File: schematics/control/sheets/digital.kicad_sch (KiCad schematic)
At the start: 17 parts, among them U1 Pico, U12 TL072, U3 MCP4822

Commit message: Updated VCA
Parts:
- added C32, C33: 100n, Shmoergh_Manual_PCB:C_Disc_D5.0mm_W2.5mm_P2.50mm, symbol Device:C
- added C34, C35, C36, C37: 100n, symbol Device:C
- added J_ADC_INPUTS1, J_BUTTON_INPUTS2: Conn_01x08_Male, Shmoergh_Manual_PCB:NSL25_01x08_Vertical, symbol Connector:Conn_01x08_Male
- added RV_ENV_GAIN1: 200k, symbol Device:R_Potentiometer_Trim
- added TP_ENV_OUT1, TP_FILT_MOD1: TestPoint, symbol Connector:TestPoint
- added U13, U14: CD4051B, Shmoergh_Manual_PCB:DIP-16_W7.62mm, symbol Analog_Switch:CD4051B
- R54: value 100k -> 22k
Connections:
- net +5V: now also C32.1, C33.1, U13.16 (VDD), U14.16 (VDD)
- net ENVELOPE: now also RV_ENV_GAIN1.1, TP_ENV_OUT1.1; no longer R54.2
- net FILTER_MOD: now also TP_FILT_MOD1.1
- net GND: now also C32.2, C33.2, C34.2, C35.2, C36.2, C37.2, U13.6 (INH), U13.7 (VEE), U13.8 (VSS), U14.6 (INH), U14.7 (VEE), U14.8 (VSS)
- net MUX_BTN: now reaches U1.11 (GPIO8)
- net MUX_BTN: now also U14.3 (X)
- net MUX_ADC: now reaches U1.31 (GPIO26_ADC0)
- net MUX_ADC: now also U13.3 (X)
- net MUX_A: now reaches U1.4 (GPIO2)
- net MUX_A: now also U13.11 (A), U14.11 (A)
- net MUX_B: now reaches U1.5 (GPIO3)
- net MUX_B: now also U13.10 (B), U14.10 (B)
- net MUX_C: now reaches U1.6 (GPIO4)
- net MUX_C: now also U13.9 (C), U14.9 (C)
- new net: R54.2, RV_ENV_GAIN1.2, RV_ENV_GAIN1.3
- new net: J_ADC_INPUTS1.8 (Pin_8), U13.4 (X7)
- new net: J_BUTTON_INPUTS2.8 (Pin_8), U14.4 (X7)
- new net DETUNE: J_BUTTON_INPUTS2.5 (Pin_5), U14.1 (X4)
- new net GLIDE: J_BUTTON_INPUTS2.4 (Pin_4), U14.12 (X3)
- new net HOLD: J_BUTTON_INPUTS2.2 (Pin_2), U14.14 (X1)
- new net KB_TRACKING: J_BUTTON_INPUTS2.6 (Pin_6), U14.5 (X5)
- new net MODE: C35.1, J_ADC_INPUTS1.2 (Pin_2), U13.14 (X1)
- new net MODWHEEL: J_ADC_INPUTS1.7 (Pin_7), U13.2 (X6)
- new net PITCH: J_ADC_INPUTS1.6 (Pin_6), U13.5 (X5)
- new net RING: J_BUTTON_INPUTS2.3 (Pin_3), U14.15 (X2)
- new net RING_AMNT: C36.1, J_ADC_INPUTS1.3 (Pin_3), U13.15 (X2)
- new net SOFT: J_BUTTON_INPUTS2.1 (Pin_1), U14.13 (X0)
- new net SOLO_CHORD: J_BUTTON_INPUTS2.7 (Pin_7), U14.2 (X6)
- new net TUNER: J_ADC_INPUTS1.5 (Pin_5), U13.1 (X4)
- new net WAH_SRC: C37.1, J_ADC_INPUTS1.4 (Pin_4), U13.12 (X3)
- new net WAVESHAPE: C34.1, J_ADC_INPUTS1.1 (Pin_1), U13.13 (X0)
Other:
- note added: "ADC inputs ------- Waveshape (saw/sqr/mixed) Mode (mono, 3/6 para) Ring amount Wah source Global tuner Pitch Modwheel * note: square pulse width is completely analog and set externally on the UI"
- note added: "Binary inputs (on/off) ------------- Soft Hold Ring Glide Detune Keyboard tracking Solo/chord"
- note added: "Envelope maximum: about 5-12V"
- note removed: "Envelope varies between 0-8V"
- moved on the sheet: C30, C31, J_SWD_IO?, R53, R54, R55, R56, U1, U12A, U12B, U12C, U3

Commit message: Coded portamento (untested)
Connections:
- net MUX_BTN renamed MUX_BINARY
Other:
- note added: "ADC inputs ------- Waveshape (saw/sqr/mixed) Mode (mono, 3/6 para) Ring amount Wah source Global tuner Pitch (Modwheel? — This can be pure analog) * note: square pulse width is completely analog and set externally on the UI"
- note added: "ATM it's only keyboard tracking"
- note removed: "ADC inputs ------- Waveshape (saw/sqr/mixed) Mode (mono, 3/6 para) Ring amount Wah source Global tuner Pitch Modwheel * note: square pulse width is completely analog and set externally on the UI"
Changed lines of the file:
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@@
     (stroke (width 0) (type default))
   )
+  (text "ATM it's only keyboard \ntracking" (at 177.8 121.92 0)
+    (effects (font (size 1.27 1.27)) (justify left bottom))
+  )
   (text "In Purple Thunder MIDI IN is connected to GPIO9" (at 109.22 176.53 0)
     (effects (font (size 1.27 1.27)) (justify left bottom))
@@
     (effects (font (size 1.27 1.27)) (justify left bottom))
   )
-  (text "ADC inputs\n-------\nWaveshape (saw/sqr/mixed)\nMode (mono, 3/6 para)\nRing amount\nWah source\nGlobal tuner\nPitch\nModwheel\n\n* note: square pulse width \nis completely analog and\nset externally on the UI"
-    (at 181.61 43.18 0)
+  (text "ADC inputs\n-------\nWaveshape (saw/sqr/mixed)\nMode (mono, 3/6 para)\nRing amount\nWah source\nGlobal tuner\nPitch\n(Modwheel? — This can be \npure analog)\n\n* note: square pulse width \nis completely analog and\nset externally on the UI"
+    (at 180.34 52.07 0)
     (effects (font (size 1.27 1.27)) (justify left bottom))
   )
@@
     )
   )
-  (global_label "MUX_BTN" (shape input) (at 224.79 111.76 180) (fields_autoplaced)
-    (effects (font (size 1.27 1.27)) (justify right))
-    (property "Intersheetrefs" "${INTERSHEET_REFS}" (at 213.3571 111.76 0)
+  (global_label "MUX_BINARY" (shape input) (at 224.79 111.76 180) (fields_autoplaced)
+    (effects (font (size 1.27 1.27)) (justify right))
+    (property "Intersheetrefs" "${INTERSHEET_REFS}" (at 210.2727 111.76 0)
       (effects (font (size 1.27 1.27)) (justify right) hide)
     )
@@
     )
   )
-  (global_label "MUX_BTN" (shape input) (at 31.75 57.15 180) (fields_autoplaced)
-    (effects (font (size 1.27 1.27)) (justify right))
-    (property "Intersheetrefs" "${INTERSHEET_REFS}" (at 20.3171 57.15 0)
-      (effects (font (size 1.27 1.27)) (justify right) hide)
-    )
+  (global_label "MUX_BINARY" (shape input) (at 31.75 57.15 180) (fields_autoplaced)
+    (effects (font (size 1.27 1.27)) (justify right))
+    (property "Intersheetrefs" "${INTERSHEET_REFS}" (at 17.2327 57.15 0)
+      (effects (font (size 1.27 1.27)) (justify right) hide)
+    )

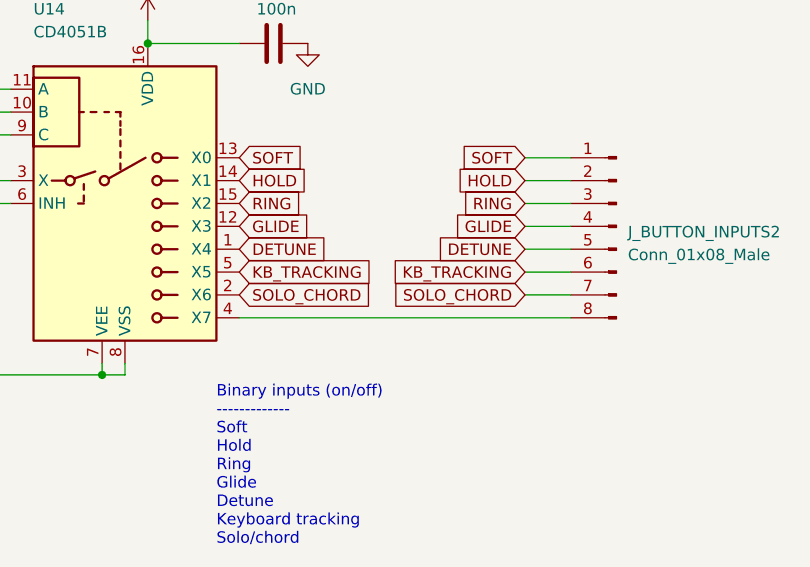
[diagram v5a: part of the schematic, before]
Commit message: Updated kb tracking for analog switch
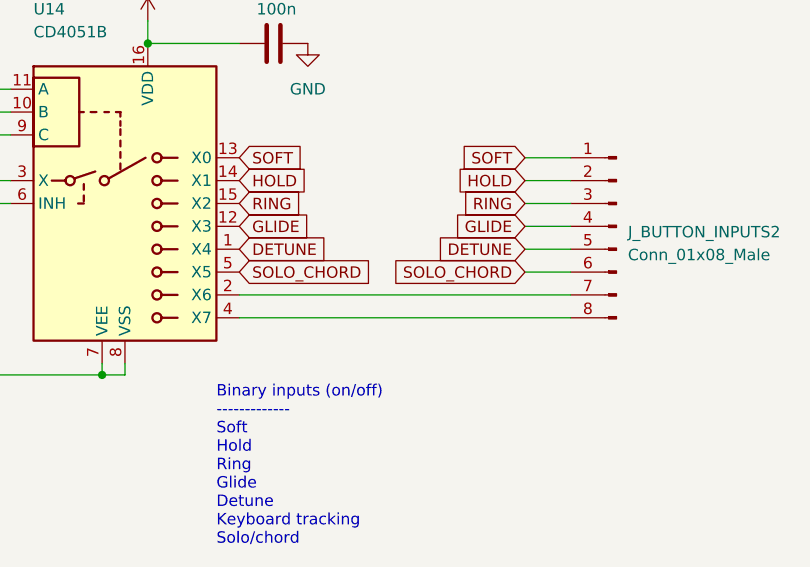
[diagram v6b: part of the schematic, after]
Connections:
- net KB_TRACKING is gone; now on net SOLO_CHORD: J_BUTTON_INPUTS2.6 (Pin_6), U14.5 (X5)
- net SOLO_CHORD: no longer J_BUTTON_INPUTS2.7 (Pin_7), U14.2 (X6)
- new net: J_BUTTON_INPUTS2.7 (Pin_7), U14.2 (X6)
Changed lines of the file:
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@@
     (stroke (width 0) (type default))
   )
-  (wire (pts (xy 283.21 124.46) (xy 288.29 124.46))
+  (wire (pts (xy 251.46 124.46) (xy 288.29 124.46))
     (stroke (width 0) (type default))
   )
@@
     )
   )
-  (global_label "SOLO_CHORD" (shape input) (at 283.21 124.46 180) (fields_autoplaced)
-    (effects (font (size 1.27 1.27)) (justify right))
-    (property "Intersheetrefs" "${INTERSHEET_REFS}" (at 267.967 124.46 0)
+  (global_label "SOLO_CHORD" (shape input) (at 283.21 121.92 180) (fields_autoplaced)
+    (effects (font (size 1.27 1.27)) (justify right))
+    (property "Intersheetrefs" "${INTERSHEET_REFS}" (at 267.967 121.92 0)
       (effects (font (size 1.27 1.27)) (justify right) hide)
     )
@@
     )
   )
-  (global_label "SOLO_CHORD" (shape input) (at 251.46 124.46 0) (fields_autoplaced)
-    (effects (font (size 1.27 1.27)) (justify left))
-    (property "Intersheetrefs" "${INTERSHEET_REFS}" (at 266.703 124.46 0)
+  (global_label "SOLO_CHORD" (shape input) (at 251.46 121.92 0) (fields_autoplaced)
+    (effects (font (size 1.27 1.27)) (justify left))
+    (property "Intersheetrefs" "${INTERSHEET_REFS}" (at 266.703 121.92 0)
       (effects (font (size 1.27 1.27)) (justify left) hide)
     )
@@
     )
   )
-  (global_label "KB_TRACKING" (shape input) (at 251.46 121.92 0) (fields_autoplaced)
-    (effects (font (size 1.27 1.27)) (justify left))
-    (property "Intersheetrefs" "${INTERSHEET_REFS}" (at 266.9449 121.92 0)
-      (effects (font (size 1.27 1.27)) (justify left) hide)
-    )
-  )
   (global_label "DAC_CS" (shape input) (at 99.06 113.03 180) (fields_autoplaced)
     (effects (font (size 1.27 1.27)) (justify right))
@@
       (effects (font (size 1.27 1.27)) (justify right) hide)
     )
-  )
-  (global_label "KB_TRACKING" (shape input) (at 283.21 121.92 180) (fields_autoplaced)
-    (effects (font (size 1.27 1.27)) (justify right))
-    (property "Intersheetrefs" "${INTERSHEET_REFS}" (at 267.7251 121.92 0)
-      (effects (font (size 1.27 1.27)) (justify right) hide)
-    )

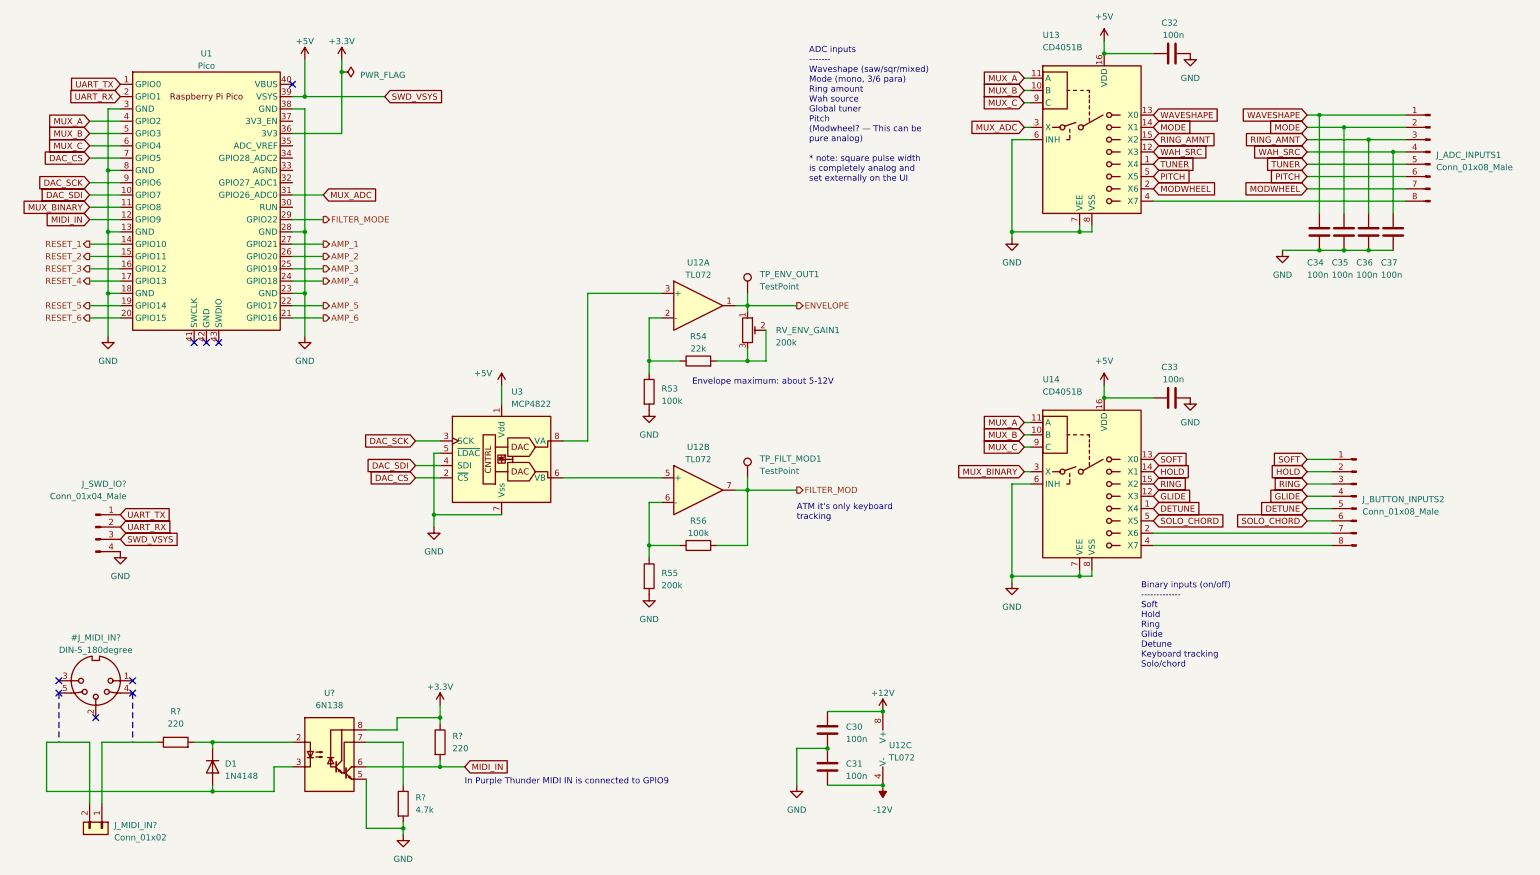
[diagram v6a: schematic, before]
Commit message: Added all UI components to schematics
- digital UI
- filter UI
- updated voice interface connection
- simplified schematics a lot
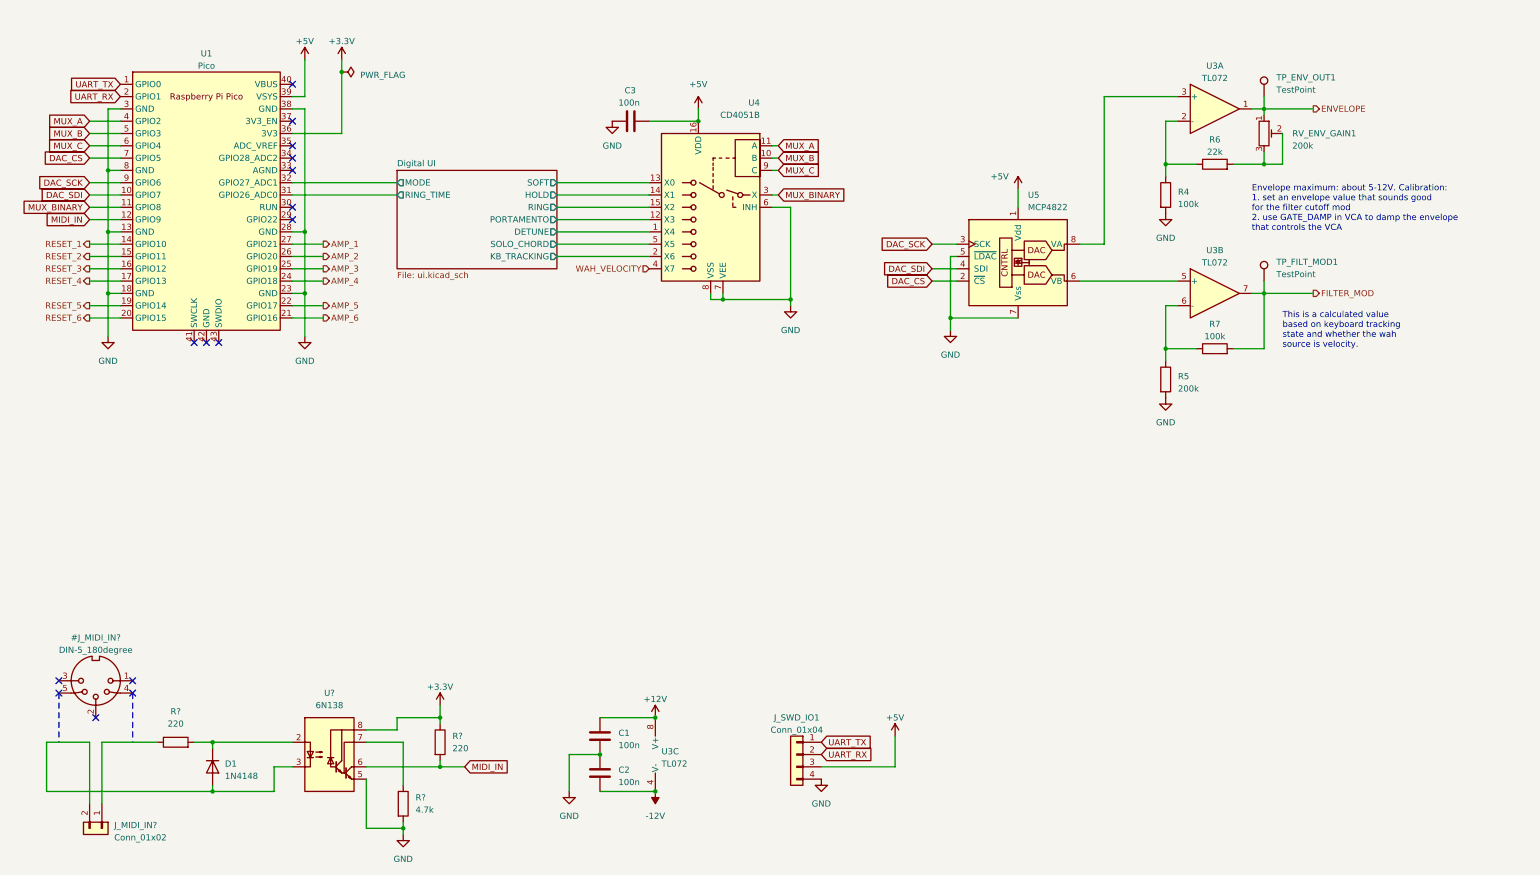
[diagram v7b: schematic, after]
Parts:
- removed C32: 100n, Shmoergh_Manual_PCB:C_Disc_D5.0mm_W2.5mm_P2.50mm, symbol Device:C
- removed C34, C35, C36, C37: 100n, symbol Device:C
- removed J_ADC_INPUTS1, J_BUTTON_INPUTS2: Conn_01x08_Male, Shmoergh_Manual_PCB:NSL25_01x08_Vertical, symbol Connector:Conn_01x08_Male
- removed J_SWD_IO?: Conn_01x04_Male, Connector_PinHeader_2.54mm:PinHeader_1x04_P2.54mm_Vertical, symbol Connector:Conn_01x04_Male
- removed U13: CD4051B, Shmoergh_Manual_PCB:DIP-16_W7.62mm, symbol Analog_Switch:CD4051B
- added J_SWD_IO1: Conn_01x04, symbol Connector_Generic:Conn_01x04
- C3: renamed from C33; footprint Shmoergh_Manual_PCB:C_Disc_D5.0mm_W2.5mm_P2.50mm -> (none)
- D1: footprint Diode_THT:D_DO-35_SOD27_P7.62mm_Horizontal -> (none)
- J_MIDI_IN?: footprint Shmoergh_Custom_Footprints:NSL25_01x02_Vertical -> (none)
- R? (x3): footprint Shmoergh_Custom_Footprints:R_Axial_DIN0207_L6.3mm_D2.5mm_P7.62mm_Horizontal -> (none)
- U1: footprint MCU_RaspberryPi_and_Boards:RPi_Pico_SMD_TH -> (none)
- U4: renamed from U14; footprint Shmoergh_Manual_PCB:DIP-16_W7.62mm -> (none)
- U5: renamed from U3; footprint Package_DIP:DIP-8_W7.62mm -> (none)
- U?: footprint Package_DIP:DIP-8_W7.62mm -> (none)
- renumbered C30 to C1, C31 to C2, R53 to R4, R55 to R5, R54 to R6, R56 to R7, U12 to U3
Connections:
- net +5V: now also J_SWD_IO1.3 (Pin_3)
- net GND: now also J_SWD_IO1.4 (Pin_4)
- net UART_RX: now also J_SWD_IO1.2 (Pin_2)
- net UART_TX: now also J_SWD_IO1.1 (Pin_1)
- net Digital UI/MODE: now reaches U1.32 (GPIO27_ADC1)
- net Digital UI/KB_TRACKING: now reaches U4.2 (X6)
- net WAH_VELOCITY: now reaches U4.4 (X7)
- net DETUNE renamed Digital UI/DETUNE
- net FILTER_MODE: no longer names the net of U1.29 (GPIO22)
- net GLIDE renamed Digital UI/PORTAMENTO
- net HOLD renamed Digital UI/HOLD
- net MUX_ADC renamed Digital UI/RING_TIME
- net RING renamed Digital UI/RING
- net SOFT renamed Digital UI/SOFT
- net SOLO_CHORD renamed Digital UI/SOLO_CHORD
- no-connect marks 9 -> 15
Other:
- added sheet Digital UI (ui.kicad_sch)
- note added: "Envelope maximum: about 5-12V. Calibration: 1. set an envelope value that sounds good for the filter cutoff mod 2. use GATE_DAMP in VCA to damp the envelope that controls the VCA"
- note added: "This is a calculated value based on keyboard tracking state and whether the wah source is velocity."
- note removed: "ADC inputs ------- Waveshape (saw/sqr/mixed) Mode (mono, 3/6 para) Ring amount Wah source Global tuner Pitch (Modwheel? — This can be pure analog) * note: square pulse width is completely analog and set externally on the UI"
- note removed: "ATM it's only keyboard tracking"
- note removed: "Binary inputs (on/off) ------------- Soft Hold Ring Glide Detune Keyboard tracking Solo/chord"
- note removed: "Envelope maximum: about 5-12V"
- note removed: "In Purple Thunder MIDI IN is connected to GPIO9"
- moved on the sheet: C1, C2, C3, R4, R5, R6, R7, RV_ENV_GAIN1, TP_ENV_OUT1, TP_FILT_MOD1, U3A, U3B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

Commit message: Refined voice values
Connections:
- net AMP_1: now also U1.21 (GPIO16); no longer U1.27 (GPIO21)
- net AMP_2: now also U1.22 (GPIO17); no longer U1.26 (GPIO20)
- net AMP_3: now also U1.24 (GPIO18); no longer U1.25 (GPIO19)
- net AMP_4: now also U1.25 (GPIO19); no longer U1.24 (GPIO18)
- net AMP_5: now also U1.26 (GPIO20); no longer U1.22 (GPIO17)
- net AMP_6: now also U1.27 (GPIO21); no longer U1.21 (GPIO16)
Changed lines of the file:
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@@
     (effects (font (size 1.27 1.27)) (justify left))
   )
-  (hierarchical_label "AMP_2" (shape output) (at 80.01 67.31 0) (fields_autoplaced)
+  (hierarchical_label "AMP_2" (shape output) (at 80.01 77.47 0) (fields_autoplaced)
     (effects (font (size 1.27 1.27)) (justify left))
   )
@@
     (effects (font (size 1.27 1.27)) (justify right))
   )
-  (hierarchical_label "AMP_3" (shape output) (at 80.01 69.85 0) (fields_autoplaced)
+  (hierarchical_label "AMP_3" (shape output) (at 80.01 72.39 0) (fields_autoplaced)
     (effects (font (size 1.27 1.27)) (justify left))
   )
@@
     (effects (font (size 1.27 1.27)) (justify left))
   )
-  (hierarchical_label "AMP_1" (shape output) (at 80.01 64.77 0) (fields_autoplaced)
+  (hierarchical_label "AMP_1" (shape output) (at 80.01 80.01 0) (fields_autoplaced)
     (effects (font (size 1.27 1.27)) (justify left))
   )
@@
     (effects (font (size 1.27 1.27)) (justify right))
   )
-  (hierarchical_label "AMP_6" (shape output) (at 80.01 80.01 0) (fields_autoplaced)
+  (hierarchical_label "AMP_6" (shape output) (at 80.01 64.77 0) (fields_autoplaced)
     (effects (font (size 1.27 1.27)) (justify left))
   )
-  (hierarchical_label "AMP_4" (shape output) (at 80.01 72.39 0) (fields_autoplaced)
+  (hierarchical_label "AMP_4" (shape output) (at 80.01 69.85 0) (fields_autoplaced)
     (effects (font (size 1.27 1.27)) (justify left))
   )
@@
     (effects (font (size 1.27 1.27)) (justify right))
   )
-  (hierarchical_label "AMP_5" (shape output) (at 80.01 77.47 0) (fields_autoplaced)
+  (hierarchical_label "AMP_5" (shape output) (at 80.01 67.31 0) (fields_autoplaced)
     (effects (font (size 1.27 1.27)) (justify left))
   )
